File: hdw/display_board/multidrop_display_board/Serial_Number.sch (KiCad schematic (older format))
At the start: 3 parts

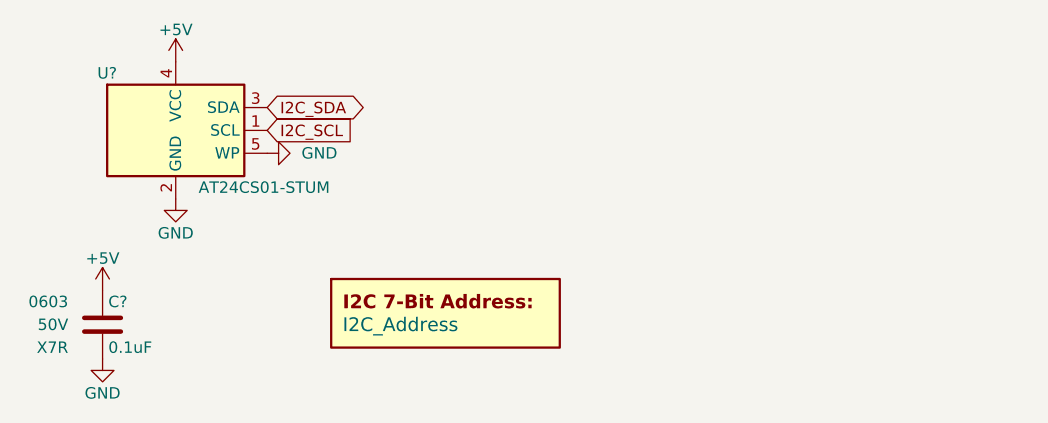
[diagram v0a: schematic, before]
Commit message: Added LED drivers, IO connectors to SCH
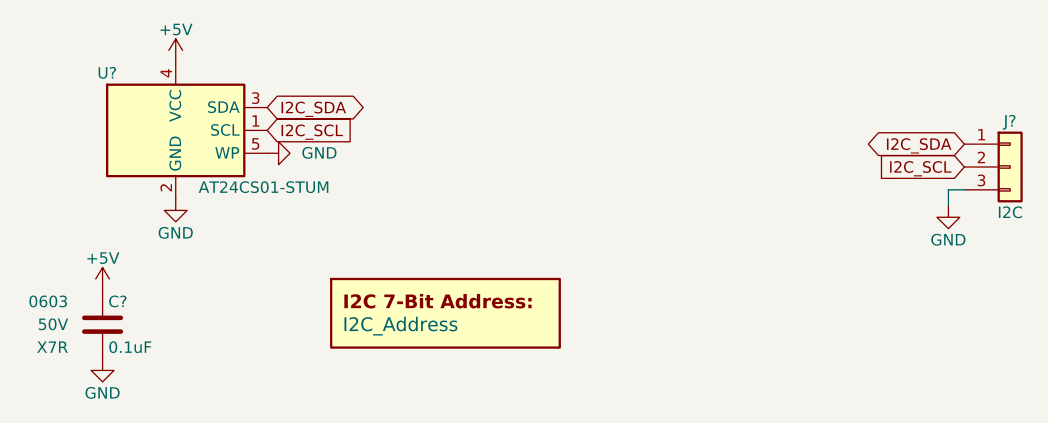
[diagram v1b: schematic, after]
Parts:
- added J?: I2C, symbol Connector_Generic:Conn_01x03
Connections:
- net GND: now also J?.3 (Pin_3)
- net I2C_SCL: now also J?.2 (Pin_2)
- net I2C_SDA: now also J?.1 (Pin_1)
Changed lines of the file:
@@
 	1    0    0    -1
 $EndComp
+Text GLabel 9010 3860 0    50   Input ~ 0
+I2C_SCL
+Text GLabel 9010 3760 0    50   BiDi ~ 0
+I2C_SDA
+$Comp
+L Connector_Generic:Conn_01x03 J?
+U 1 1 5F85F238
+P 9210 3860
+F 0 "J?" H 9210 4060 50  0000 C CNN
+F 1 "I2C" H 9210 3660 50  0000 C CNN
+F 2 "" H 9210 3860 50  0001 C CNN
+F 3 "~" H 9210 3860 50  0001 C CNN
+	1    9210 3860
+	1    0    0    -1
+$EndComp
+$Comp
+L power:GND #PWR?
+U 1 1 5F85F7CF
+P 8940 4030
+F 0 "#PWR?" H 8940 3780 50  0001 C CNN
+F 1 "GND" H 8940 3880 50  0000 C CNN
+F 2 "" H 8940 4030 50  0001 C CNN
+F 3 "" H 8940 4030 50  0001 C CNN
+	1    8940 4030
+	1    0    0    -1
+$EndComp
+Wire Wire Line
+	8940 4030 8940 3960
+Wire Wire Line
+	8940 3960 9010 3960
 $EndSCHEMATC
